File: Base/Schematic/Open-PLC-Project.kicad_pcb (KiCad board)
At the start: 2 copper layers, 122 x 87 mm, 101 parts, among them U1 MB85RC16PNF-G-JNE, U10 BTS5200-4EKA, U11 BTS5200-4EKA, U2 SL1307ZN+T, U3 M433LE8AE, U4 TPS560430XDBV, U5 TPS560430XDBV, U6 B0505S-1W, U7 CA-IS3052CW, U8 B0505S-1W, U9 CA-IS3082WX, X1 XKXGI-SUA-32.768K, X2 1532H4-12000JWPDTSNL

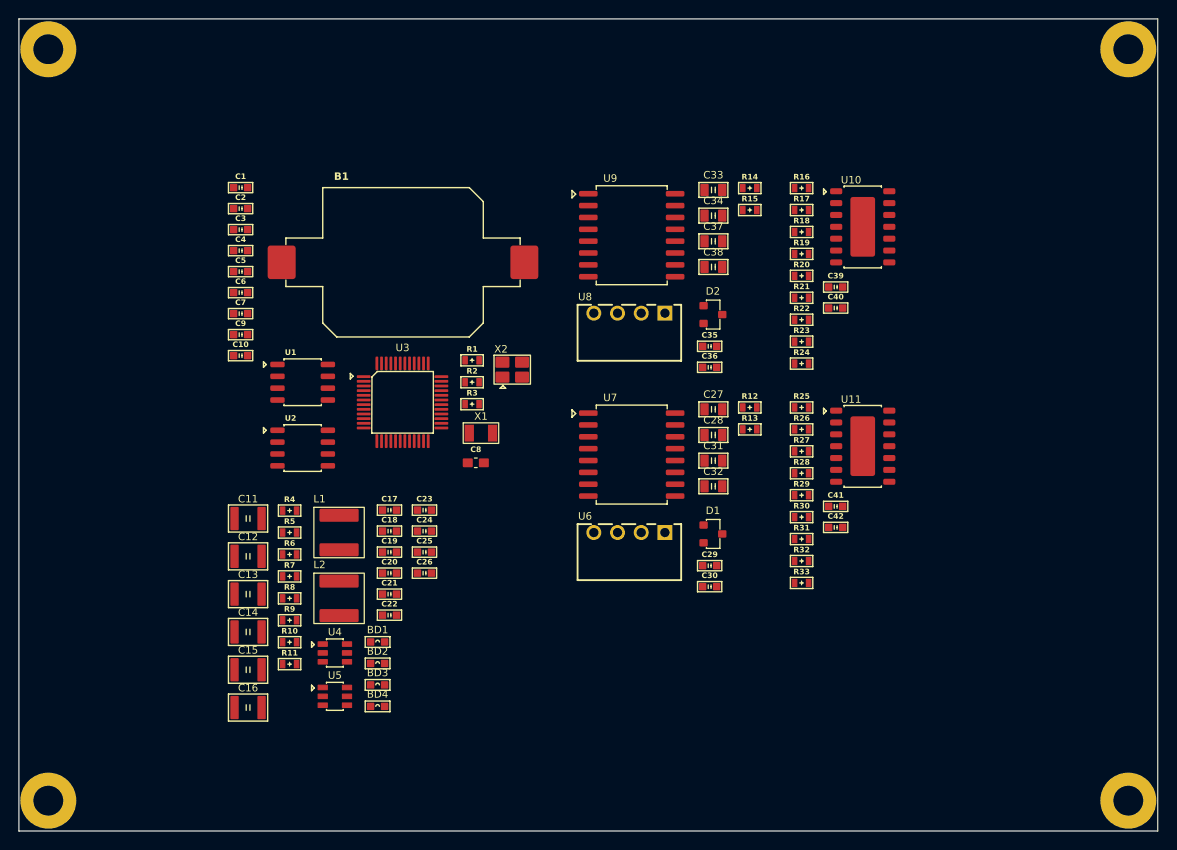
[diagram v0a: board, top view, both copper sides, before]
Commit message: [Base 회로도 업데이트] - AIN 입력 4개 추가
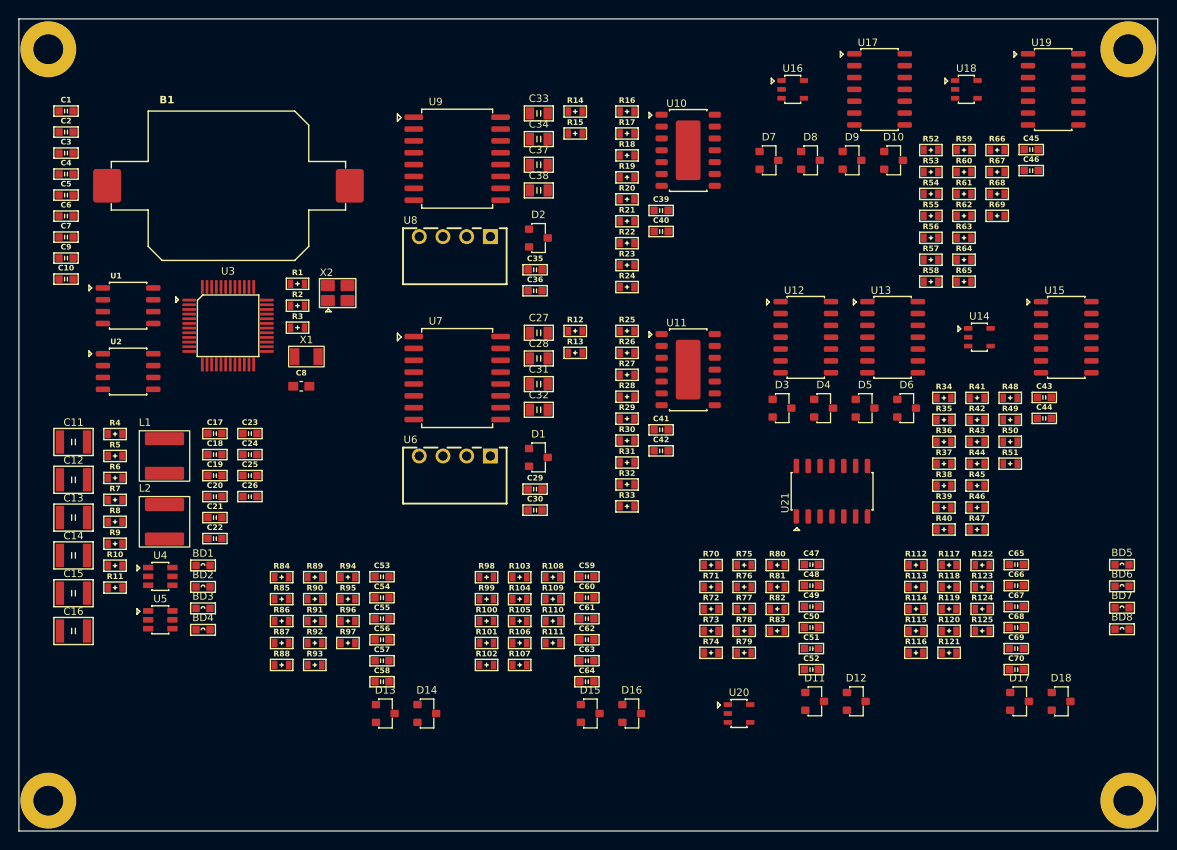
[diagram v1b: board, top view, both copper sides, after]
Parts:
- added BD5: BLM18KG121TN1D, SML:0603, F.Cu at (211.2, 104.5)
- added BD6: BLM18KG121TN1D, SML:0603, F.Cu at (211.2, 106.8)
- added BD7: BLM18KG121TN1D, SML:0603, F.Cu at (211.2, 109.1)
- added BD8: BLM18KG121TN1D, SML:0603, F.Cu at (211.2, 111.4)
- added C43: 0603B104K500, SMC:0603, F.Cu at (202.8, 86.5)
- added C44: 0603B104K500, SMC:0603, F.Cu at (202.8, 88.8)
- added C45: 0603B104K500, SMC:0603, F.Cu at (201.4, 60.0)
- added C46: 0603B104K500, SMC:0603, F.Cu at (201.4, 62.2)
- added C47: 0603B104K500, SMC:0603, F.Cu at (177.9, 104.5)
- added C48: 0603B101K500, SMC:0603, F.Cu at (177.9, 106.7)
- added C49: 0603B101K500, SMC:0603, F.Cu at (177.9, 109.0)
- added C50: 0603B101K500, SMC:0603, F.Cu at (177.9, 111.2)
- added C51: 0603B104K500, SMC:0603, F.Cu at (177.9, 113.5)
- added C52: 0603B104K500, SMC:0603, F.Cu at (177.9, 115.7)
- added C53: 0603B104K500, SMC:0603, F.Cu at (131.9, 105.8)
- added C54: 0603B101K500, SMC:0603, F.Cu at (131.9, 108.0)
- added C55: 0603B101K500, SMC:0603, F.Cu at (131.9, 110.3)
- added C56: 0603B101K500, SMC:0603, F.Cu at (131.9, 112.5)
- added C57: 0603B104K500, SMC:0603, F.Cu at (131.9, 114.8)
- added C58: 0603B104K500, SMC:0603, F.Cu at (131.9, 117.0)
- added C59: 0603B104K500, SMC:0603, F.Cu at (153.8, 105.8)
- added C60: 0603B101K500, SMC:0603, F.Cu at (153.8, 108.0)
- added C61: 0603B101K500, SMC:0603, F.Cu at (153.8, 110.3)
- added C62: 0603B101K500, SMC:0603, F.Cu at (153.8, 112.5)
- added C63: 0603B104K500, SMC:0603, F.Cu at (153.8, 114.8)
- added C64: 0603B104K500, SMC:0603, F.Cu at (153.8, 117.0)
- added C65: 0603B104K500, SMC:0603, F.Cu at (199.8, 104.5)
- added C66: 0603B101K500, SMC:0603, F.Cu at (199.8, 106.7)
- added C67: 0603B101K500, SMC:0603, F.Cu at (199.8, 109.0)
- added C68: 0603B101K500, SMC:0603, F.Cu at (199.8, 111.2)
- added C69: 0603B104K500, SMC:0603, F.Cu at (199.8, 113.5)
- added C70: 0603B104K500, SMC:0603, F.Cu at (199.8, 115.7)
- added D10: KDS226, SOT:SOT23, F.Cu at (186.7, 61.1)
- added D11: KDS226, SOT:SOT23, F.Cu at (178.2, 119.1)
- added D12: KDS226, SOT:SOT23, F.Cu at (182.7, 119.1)
- added D13: KDS226, SOT:SOT23, F.Cu at (132.2, 120.4)
- added D14: KDS226, SOT:SOT23, F.Cu at (136.7, 120.4)
- added D15: KDS226, SOT:SOT23, F.Cu at (154.2, 120.4)
- added D16: KDS226, SOT:SOT23, F.Cu at (158.7, 120.4)
- added D17: KDS226, SOT:SOT23, F.Cu at (200.2, 119.1)
- added D18: KDS226, SOT:SOT23, F.Cu at (204.7, 119.1)
- added D3: KDS226, SOT:SOT23, F.Cu at (174.8, 87.7)
- added D4: KDS226, SOT:SOT23, F.Cu at (179.2, 87.7)
- added D5: KDS226, SOT:SOT23, F.Cu at (183.7, 87.7)
- added D6: KDS226, SOT:SOT23, F.Cu at (188.1, 87.7)
- added D7: KDS226, SOT:SOT23, F.Cu at (173.3, 61.1)
- added D8: KDS226, SOT:SOT23, F.Cu at (177.8, 61.1)
- added D9: KDS226, SOT:SOT23, F.Cu at (182.2, 61.1)
- added R100: WR06X1002FTL, SMR:0603, F.Cu at (143.1, 110.5)
- added R101: WR06X1002FTL, SMR:0603, F.Cu at (143.1, 112.9)
- added R102: WR06X3302FTL, SMR:0603, F.Cu at (143.1, 115.2)
- added R103: WR06X3302FTL, SMR:0603, F.Cu at (146.7, 105.8)
- added R104: WR06X3302FTL, SMR:0603, F.Cu at (146.7, 108.2)
- added R105: WR06X3302FTL, SMR:0603, F.Cu at (146.7, 110.5)
- added R106: WR06X1002FTL, SMR:0603, F.Cu at (146.7, 112.9)
- added R107: WR06X1002FTL, SMR:0603, F.Cu at (146.7, 115.2)
- added R108: WR06X1002FTL, SMR:0603, F.Cu at (150.2, 105.8)
- added R109: WR06X1002FTL, SMR:0603, F.Cu at (150.2, 108.2)
- added R110: WR06X1001FTL, SMR:0603, F.Cu at (150.2, 110.5)
- added R111: WR06X1001FTL, SMR:0603, F.Cu at (150.2, 112.9)
- added R112: WR06X1002FTL, SMR:0603, F.Cu at (189.1, 104.5)
- added R113: WR06X1002FTL, SMR:0603, F.Cu at (189.1, 106.9)
- added R114: WR06X1002FTL, SMR:0603, F.Cu at (189.1, 109.2)
- added R115: WR06X1002FTL, SMR:0603, F.Cu at (189.1, 111.6)
- added R116: WR06X3302FTL, SMR:0603, F.Cu at (189.1, 113.9)
- added R117: WR06X3302FTL, SMR:0603, F.Cu at (192.7, 104.5)
- added R118: WR06X3302FTL, SMR:0603, F.Cu at (192.7, 106.9)
- added R119: WR06X3302FTL, SMR:0603, F.Cu at (192.7, 109.2)
- added R120: WR06X1002FTL, SMR:0603, F.Cu at (192.7, 111.6)
- added R121: WR06X1002FTL, SMR:0603, F.Cu at (192.7, 113.9)
- added R122: WR06X1002FTL, SMR:0603, F.Cu at (196.2, 104.5)
- added R123: WR06X1002FTL, SMR:0603, F.Cu at (196.2, 106.9)
- added R124: WR06X1001FTL, SMR:0603, F.Cu at (196.2, 109.2)
- added R125: WR06X1001FTL, SMR:0603, F.Cu at (196.2, 111.6)
- added R34: WR06X4701FTL, SMR:0603, F.Cu at (192.1, 86.6)
- added R35: WR06X4700FTL, SMR:0603, F.Cu at (192.1, 89.0)
- added R36: WR06X4701FTL, SMR:0603, F.Cu at (192.1, 91.3)
- added R37: WR06X4701FTL, SMR:0603, F.Cu at (192.1, 93.7)
- added R38: WR06X4701FTL, SMR:0603, F.Cu at (192.1, 96.0)
- added R39: WR06X4701FTL, SMR:0603, F.Cu at (192.1, 98.3)
- added R40: WR06X4701FTL, SMR:0603, F.Cu at (192.1, 100.7)
- added R41: WR06X4701FTL, SMR:0603, F.Cu at (195.7, 86.6)
- added R42: WR06X4701FTL, SMR:0603, F.Cu at (195.7, 89.0)
- added R43: WR06X4701FTL, SMR:0603, F.Cu at (195.7, 91.3)
- added R44: WR06X4701FTL, SMR:0603, F.Cu at (195.7, 93.7)
- added R45: WR06X4701FTL, SMR:0603, F.Cu at (195.7, 96.0)
- added R46: WR06X4701FTL, SMR:0603, F.Cu at (195.7, 98.3)
- added R47: WR06X4701FTL, SMR:0603, F.Cu at (195.7, 100.7)
- added R48: WR06X1002FTL, SMR:0603, F.Cu at (199.2, 86.6)
- added R49: WR06X1002FTL, SMR:0603, F.Cu at (199.2, 89.0)
- added R50: WR06X1002FTL, SMR:0603, F.Cu at (199.2, 91.3)
- added R51: WR06X1002FTL, SMR:0603, F.Cu at (199.2, 93.7)
- added R52: WR06X4701FTL, SMR:0603, F.Cu at (190.7, 60.0)
- added R53: WR06X4700FTL, SMR:0603, F.Cu at (190.7, 62.4)
- added R54: WR06X4701FTL, SMR:0603, F.Cu at (190.7, 64.8)
- added R55: WR06X4701FTL, SMR:0603, F.Cu at (190.7, 67.1)
- added R56: WR06X4701FTL, SMR:0603, F.Cu at (190.7, 69.5)
- added R57: WR06X4701FTL, SMR:0603, F.Cu at (190.7, 71.8)
- added R58: WR06X4701FTL, SMR:0603, F.Cu at (190.7, 74.2)
- added R59: WR06X4701FTL, SMR:0603, F.Cu at (194.2, 60.0)
- added R60: WR06X4701FTL, SMR:0603, F.Cu at (194.2, 62.4)
- added R61: WR06X4701FTL, SMR:0603, F.Cu at (194.2, 64.8)
- added R62: WR06X4701FTL, SMR:0603, F.Cu at (194.2, 67.1)
- added R63: WR06X4701FTL, SMR:0603, F.Cu at (194.2, 69.5)
- added R64: WR06X4701FTL, SMR:0603, F.Cu at (194.2, 71.8)
- added R65: WR06X4701FTL, SMR:0603, F.Cu at (194.2, 74.2)
- added R66: WR06X1002FTL, SMR:0603, F.Cu at (197.8, 60.0)
- added R67: WR06X1002FTL, SMR:0603, F.Cu at (197.8, 62.4)
- added R68: WR06X1002FTL, SMR:0603, F.Cu at (197.8, 64.8)
- added R69: WR06X1002FTL, SMR:0603, F.Cu at (197.8, 67.1)
- added R70: WR06X1002FTL, SMR:0603, F.Cu at (167.2, 104.5)
- added R71: WR06X1002FTL, SMR:0603, F.Cu at (167.2, 106.9)
- added R72: WR06X1002FTL, SMR:0603, F.Cu at (167.2, 109.2)
- added R73: WR06X1002FTL, SMR:0603, F.Cu at (167.2, 111.6)
- added R74: WR06X3302FTL, SMR:0603, F.Cu at (167.2, 113.9)
- added R75: WR06X3302FTL, SMR:0603, F.Cu at (170.7, 104.5)
- added R76: WR06X3302FTL, SMR:0603, F.Cu at (170.7, 106.9)
- added R77: WR06X3302FTL, SMR:0603, F.Cu at (170.7, 109.2)
- added R78: WR06X1002FTL, SMR:0603, F.Cu at (170.7, 111.6)
- added R79: WR06X1002FTL, SMR:0603, F.Cu at (170.7, 113.9)
- added R80: WR06X1002FTL, SMR:0603, F.Cu at (174.2, 104.5)
- added R81: WR06X1002FTL, SMR:0603, F.Cu at (174.2, 106.9)
- added R82: WR06X1001FTL, SMR:0603, F.Cu at (174.2, 109.2)
- added R83: WR06X1001FTL, SMR:0603, F.Cu at (174.2, 111.6)
- added R84: WR06X1002FTL, SMR:0603, F.Cu at (121.2, 105.8)
- added R85: WR06X1002FTL, SMR:0603, F.Cu at (121.2, 108.2)
- added R86: WR06X1002FTL, SMR:0603, F.Cu at (121.2, 110.5)
- added R87: WR06X1002FTL, SMR:0603, F.Cu at (121.2, 112.9)
- added R88: WR06X3302FTL, SMR:0603, F.Cu at (121.2, 115.2)
- added R89: WR06X3302FTL, SMR:0603, F.Cu at (124.7, 105.8)
- added R90: WR06X3302FTL, SMR:0603, F.Cu at (124.7, 108.2)
- added R91: WR06X3302FTL, SMR:0603, F.Cu at (124.7, 110.5)
- added R92: WR06X1002FTL, SMR:0603, F.Cu at (124.7, 112.9)
- added R93: WR06X1002FTL, SMR:0603, F.Cu at (124.7, 115.2)
- added R94: WR06X1002FTL, SMR:0603, F.Cu at (128.2, 105.8)
- added R95: WR06X1002FTL, SMR:0603, F.Cu at (128.2, 108.2)
- added R96: WR06X1001FTL, SMR:0603, F.Cu at (128.2, 110.5)
- added R97: WR06X1001FTL, SMR:0603, F.Cu at (128.2, 112.9)
- added R98: WR06X1002FTL, SMR:0603, F.Cu at (143.1, 105.8)
- added R99: WR06X1002FTL, SMR:0603, F.Cu at (143.1, 108.2)
- added U12: LM239DR2G, SO:SOIC-14, F.Cu at (177.3, 80.1)
- added U13: LM239DR2G, SO:SOIC-14, F.Cu at (186.6, 80.1)
- added U14: LMV321-TR, SOT:SOT-23-5L, F.Cu at (195.9, 80.1)
- added U15: TP2584-SR, SO:SOIC-14, F.Cu at (205.2, 80.1)
- added U16: LMV321-TR, SOT:SOT-23-5L, F.Cu at (175.9, 53.5)
- added U17: TP2584-SR, SO:SOIC-14, F.Cu at (185.2, 53.5)
- added U18: LMV321-TR, SOT:SOT-23-5L, F.Cu at (194.5, 53.5)
- added U19: TP2584-SR, SO:SOIC-14, F.Cu at (203.8, 53.5)
- added U20: LMV321-TR, SOT:SOT-23-5L, F.Cu at (170.2, 120.4)
- added U21: TP2584-SR, SO:SOIC-14, F.Cu at (180.1, 96.6)
- moved BD1 20.4 mm to (112.7, 104.5)
- moved BD2 20.4 mm to (112.7, 106.8)
- moved BD4 20.4 mm to (112.7, 111.5)
- moved C27 20.4 mm to (148.7, 79.6)
- moved C28 20.4 mm to (148.7, 82.4)
- moved C31 20.4 mm to (148.7, 85.1)
- moved C32 20.4 mm to (148.7, 87.9)
- moved C33 20.4 mm to (148.7, 56.1)
- moved C34 20.4 mm to (148.7, 58.9)
- moved C37 20.4 mm to (148.7, 61.6)
- moved C38 20.4 mm to (148.7, 64.4)
- moved R1 20.4 mm to (122.8, 74.4)
- moved R12 20.4 mm to (152.6, 79.4)
- moved R14 20.4 mm to (152.6, 55.9)
- moved R2 20.4 mm to (122.8, 76.7)
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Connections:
- BD3 pad 1: Net-(BD3-Pad1) -> V_SUPPLY
- BD3 pad 2: +3.3V -> A_V_SUPPLY
- BD4 pad 2: GND -> AGND
- C22 pad 2: Net-(BD3-Pad1) -> Net-(BD7-Pad1)
- C24 pad 2: Net-(BD3-Pad1) -> Net-(BD7-Pad1)
- C26 pad 2: Net-(BD3-Pad1) -> Net-(BD7-Pad1)
- L2 pad 2: Net-(BD3-Pad1) -> Net-(BD7-Pad1)
- R10 pad 2: Net-(BD3-Pad1) -> Net-(BD7-Pad1)
- U3 pad 46: GND -> AGND
